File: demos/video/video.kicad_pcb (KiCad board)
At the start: 4 copper layers, 312 x 106.7 mm, 189 parts, among them J4 DB9FEM, P1 BNC, P10 CONN_1, P11 CONN_1, P12 CONN_1, P2 BNC, P3 BNC, P4 CONN_2, P5 CONN_5, P8 BNC, P9 CONN_1, Q1 BC848, Q2 BC848, Q3 BC848, U1 24C16, U10 BT812, U11 S5933_PQ160, U12 SIM4X32, U13 SIM4X32, U14 SIM4X32, U15 SIM4X32, U16 SIM4X32, U17 SIM4X32, U18 SIM4X32, U19 SIM4X32, U2 4C4001, U20 TDA8501, U21 XC1736APD8, U22 XC4003-VQ100, U23 XC4003/PQ100, U24 XC4005-PQ160, U3 74LS245, U4 74LS245, U5 74LS245, U6 74LS245, U7 AV9173, U8 BT253, U9 BT473, X1 10MHz, X2 30MHz, X3 4,433618MH

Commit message: wip
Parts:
- moved L1 4.64 mm to (75.5, 107.0)

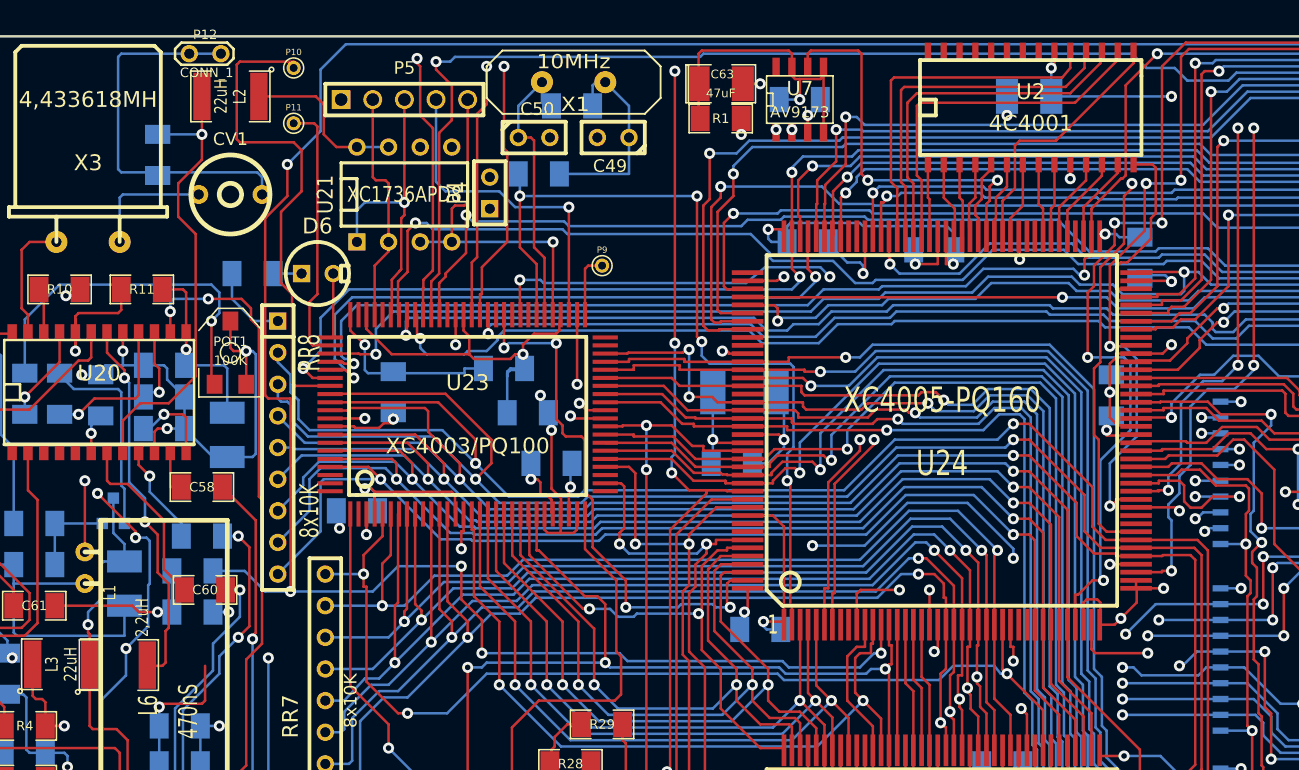
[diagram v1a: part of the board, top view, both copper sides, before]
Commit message: New connectivity algorithm.
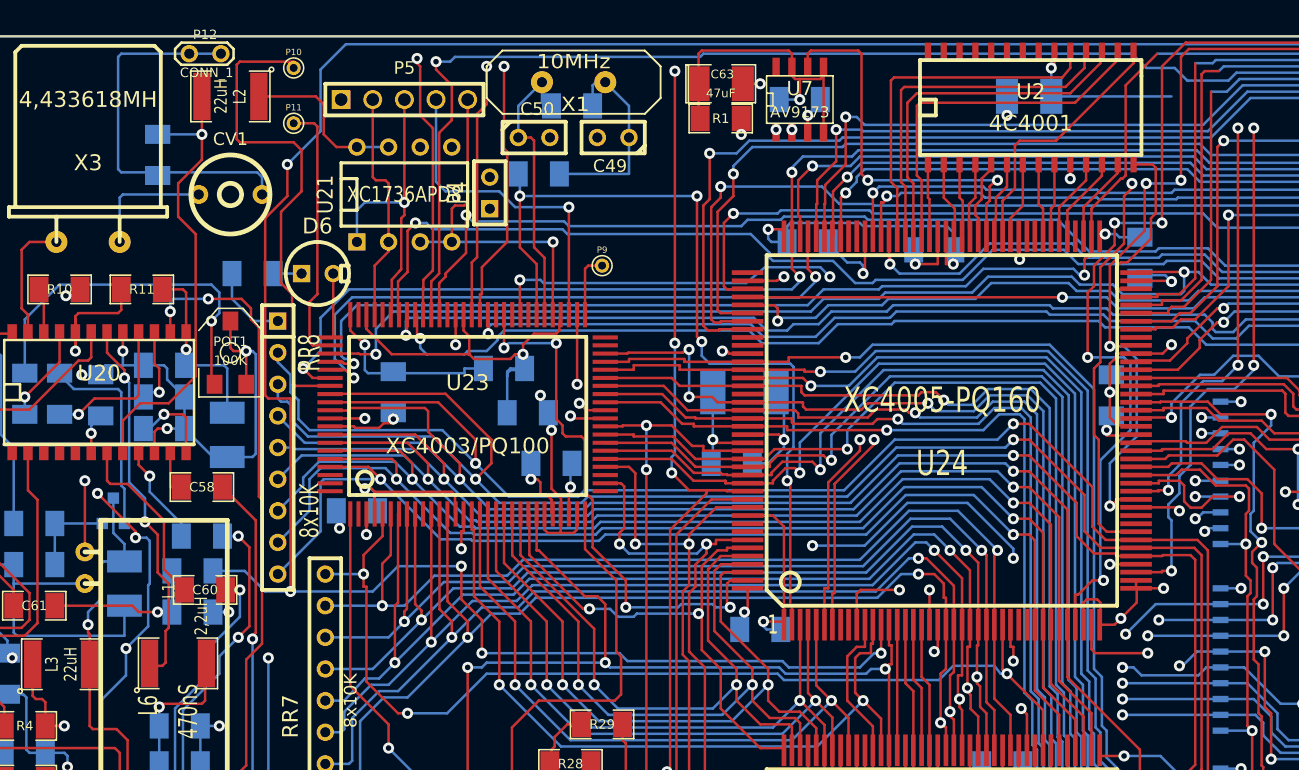
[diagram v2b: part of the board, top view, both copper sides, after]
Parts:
- moved L1 4.75 mm to (80.2, 106.9)
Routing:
- net GND: vias 104 -> 103
- net /graphic/X_PROG-: vias 4 -> 3
- net /graphic/CDACLK: vias 6 -> 5
- net /graphic/CADCLK: vias 4 -> 3
- net /ESVIDEO-RVB/CLAMP: vias 6 -> 5
